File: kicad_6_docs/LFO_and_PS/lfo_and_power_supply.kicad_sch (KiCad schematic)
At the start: 16 parts, among them SW1 sweep_mode, SW3 SW_SPDT, U4 TL072

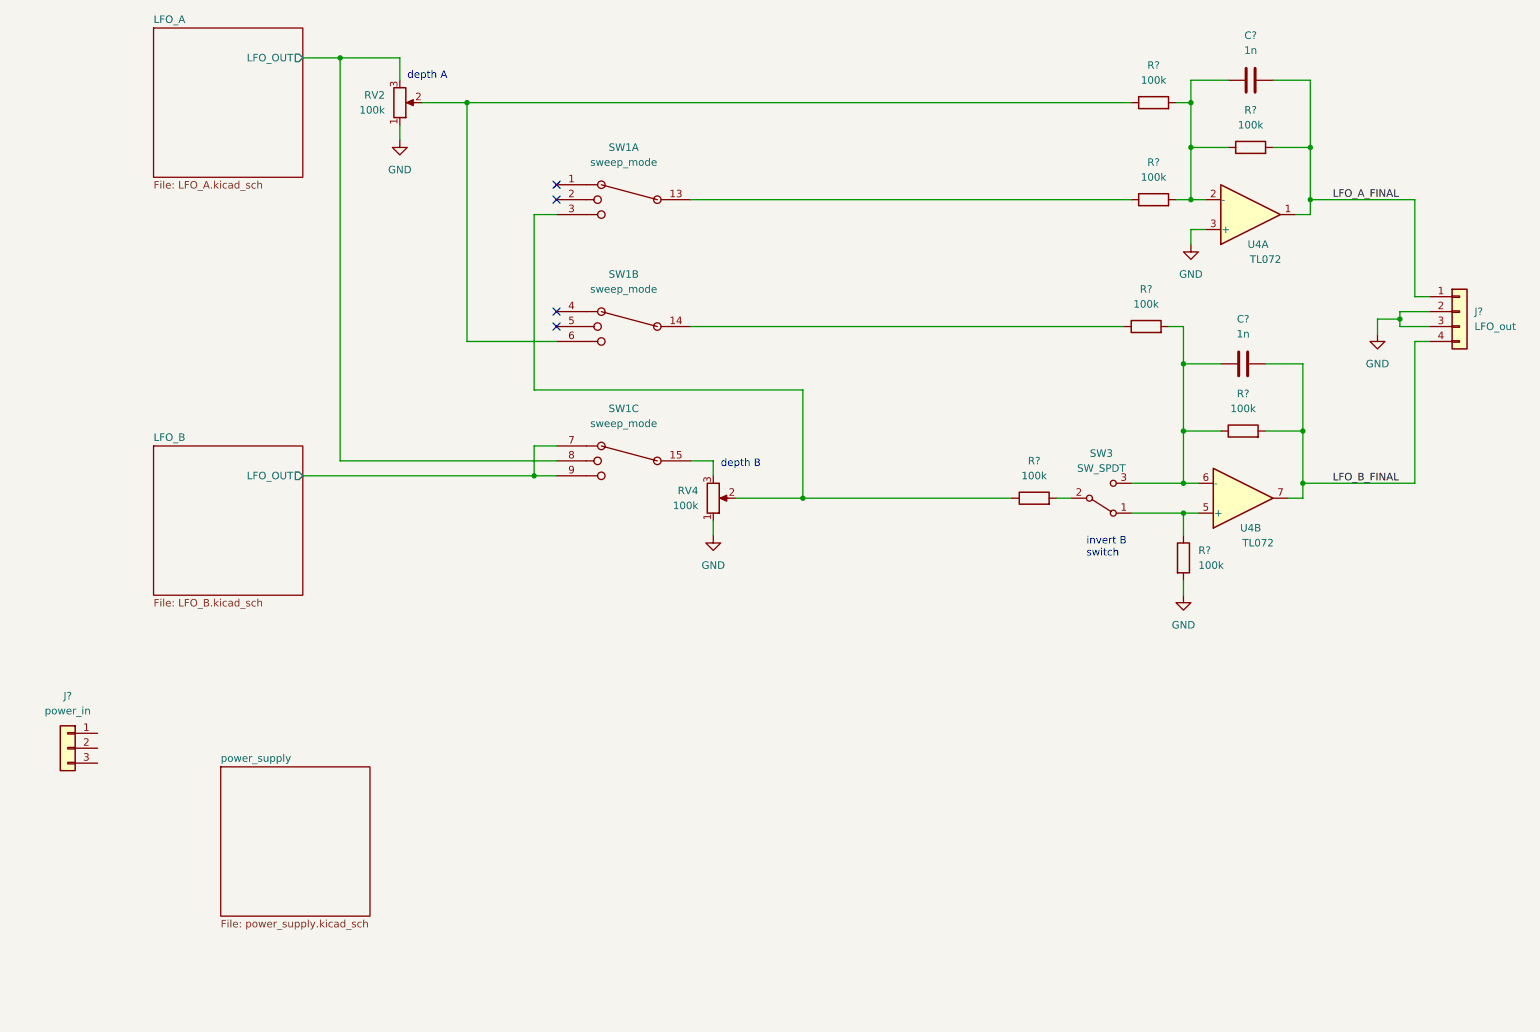
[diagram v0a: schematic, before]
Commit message: Progress on LFO/PS board
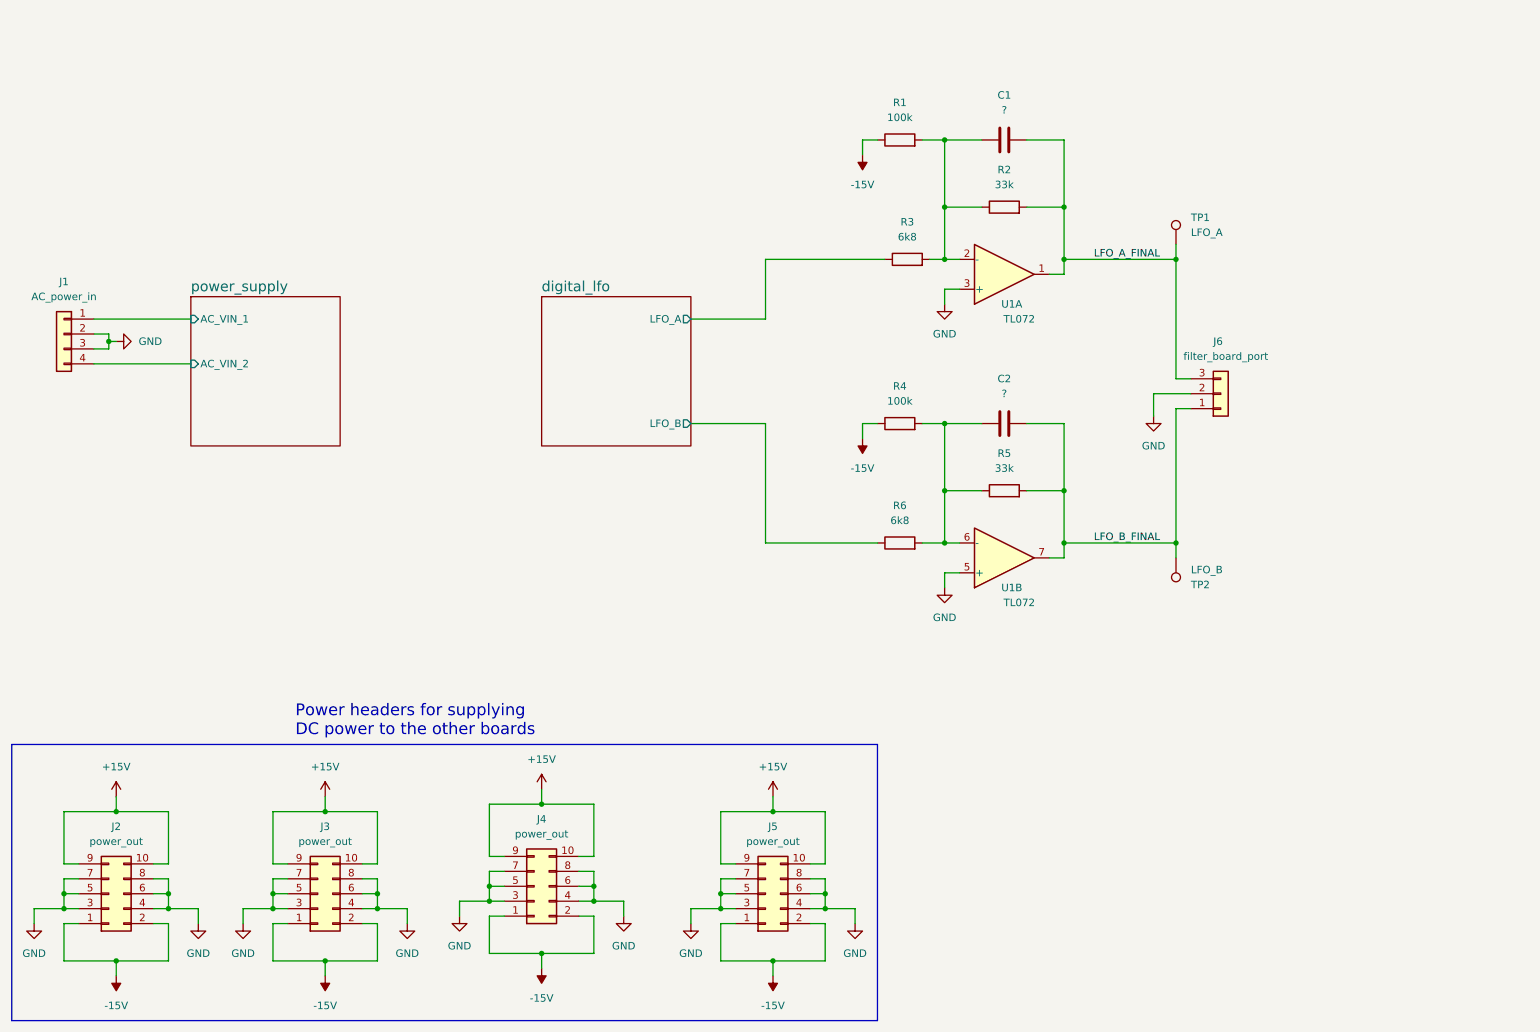
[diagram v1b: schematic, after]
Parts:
- removed J?: LFO_out, symbol Connector_Generic:Conn_01x04
- removed J?: power_in, symbol Connector_Generic:Conn_01x03
- removed R? (x4): 100k, symbol Device:R
- removed RV2, RV4: 100k, symbol Device:R_Potentiometer
- removed SW1: sweep_mode, symbol custom_symbols:SW_Rotary4x3
- removed SW3: SW_SPDT, symbol Switch:SW_SPDT
- added J1: AC_power_in, Connector_Molex:Molex_Mini-Fit_Jr_5566-04A2_2x02_P4.20mm_Vertical, symbol Connector_Generic:Conn_01x04
- added J2, J3, J4, J5: power_out, Connector_IDC:IDC-Header_2x05_P2.54mm_Vertical, symbol Connector_Generic:Conn_02x05_Odd_Even
- added J6: filter_board_port, Connector_Molex:Molex_KK-254_AE-6410-03A_1x03_P2.54mm_Vertical, symbol Connector_Generic:Conn_01x03
- added R1, R4: 100k, Resistor_SMD:R_0805_2012Metric, symbol Device:R
- added R6: 6k8, Resistor_SMD:R_0805_2012Metric, symbol Device:R
- added TP1: LFO_A, TestPoint:TestPoint_Keystone_5000-5004_Miniature, symbol Connector:TestPoint
- added TP2: LFO_B, TestPoint:TestPoint_Keystone_5000-5004_Miniature, symbol Connector:TestPoint
- C1, C2: renamed from C?; value 1n -> ?; footprint (none) -> Capacitor_SMD:C_0805_2012Metric
- R2, R5: renamed from R?; value 100k -> 33k; footprint (none) -> Resistor_SMD:R_0805_2012Metric
- R3: renamed from R?; value 100k -> 6k8; footprint (none) -> Resistor_SMD:R_0805_2012Metric
- U1: renamed from U4; footprint (none) -> Package_SO:SOIC-8_3.9x4.9mm_P1.27mm
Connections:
- net GND: now also U1.5 (+), J1.2 (Pin_2), J1.3 (Pin_3), J2.3 (Pin_3), J2.4 (Pin_4), J2.5 (Pin_5), J2.6 (Pin_6), J2.7 (Pin_7), J2.8 (Pin_8), J3.3 (Pin_3), J3.4 (Pin_4), J3.5 (Pin_5), J3.6 (Pin_6), J3.7 (Pin_7), J3.8 (Pin_8), J4.3 (Pin_3), J4.4 (Pin_4), J4.5 (Pin_5), J4.6 (Pin_6), J4.7 (Pin_7), J4.8 (Pin_8), J5.3 (Pin_3), J5.4 (Pin_4), J5.5 (Pin_5), J5.6 (Pin_6), J5.7 (Pin_7), J5.8 (Pin_8), J6.2 (Pin_2)
- net LFO_A_FINAL: now also J6.3 (Pin_3), TP1.1
- net LFO_B_FINAL: now also J6.1 (Pin_1), TP2.1
- net at C2.1, R5.1, U1.6 (-): now also R4.2, R6.2
- net at C1.1, R2.1, R3.2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: now also R1.2
- net digital_lfo/LFO_A: now reaches R3.1
- new net +15V: J2.10 (Pin_10), J2.9 (Pin_9), J3.10 (Pin_10), J3.9 (Pin_9), J4.10 (Pin_10), J4.9 (Pin_9), J5.10 (Pin_10), J5.9 (Pin_9)
- new net -15V: J2.1 (Pin_1), J2.2 (Pin_2), J3.1 (Pin_1), J3.2 (Pin_2), J4.1 (Pin_1), J4.2 (Pin_2), J5.1 (Pin_1), J5.2 (Pin_2), R1.1, R4.1
- new net digital_lfo/LFO_B: R6.1
- new net power_supply/AC_VIN_1: J1.1 (Pin_1)
- new net power_supply/AC_VIN_2: J1.4 (Pin_4)
- no-connect marks 4 -> 0
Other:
- removed sheet LFO_A
- removed sheet LFO_B
- added sheet digital_lfo (digital_lfo.kicad_sch)
- sheet power_supply ports: added AC_VIN_1, AC_VIN_2; removed none
- note added: "Power headers for supplying DC power to the other boards"
- note removed: "depth A"
- note removed: "depth B"
- note removed: "invert B switch"
- moved on the sheet: C1, C2, R2, R3, R5, U1A, U1B
